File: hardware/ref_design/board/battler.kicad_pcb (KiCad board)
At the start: 2 copper layers, 71.4 x 127.7 mm, 173 parts, among them J1 TYPE-C-31-M-12, J2 53261-0271, J3 FH12-50S-0.5SH(55), J4 53261-0271, J5 SWD, J6 UART, J7 DEBUG PADS, Q1 2N7002, Q2 AO3401A, Q3 2N7002, Q4 2N7002, Q5 AO3400A, Q6 AO3400A, SW1 P1 UP, SW10 P2 DOWN, SW11 P2 LEFT, SW12 P2 RIGHT, SW13 P2 A, SW14 P2 B, SW15 P2 X, SW16 P2 Y, SW18 BOOTSEL, SW19 RESET, SW2 P1 DOWN, SW20 P1 SELECT, SW21 P1 START / PWR, SW22 P2 SELECT, SW23 P2 START, SW3 P1 LEFT, SW4 P1 RIGHT, SW5 P1 A, SW6 P1 B, SW7 P1 X, SW8 P1 Y, SW9 P2 UP, U1 SRV05-4, U2 TP4056-42-ESOP8, U3 ME6211C33M5G, U4 RP2354B, U6 MCP6002, U7 FM8002A, X1 12MHz

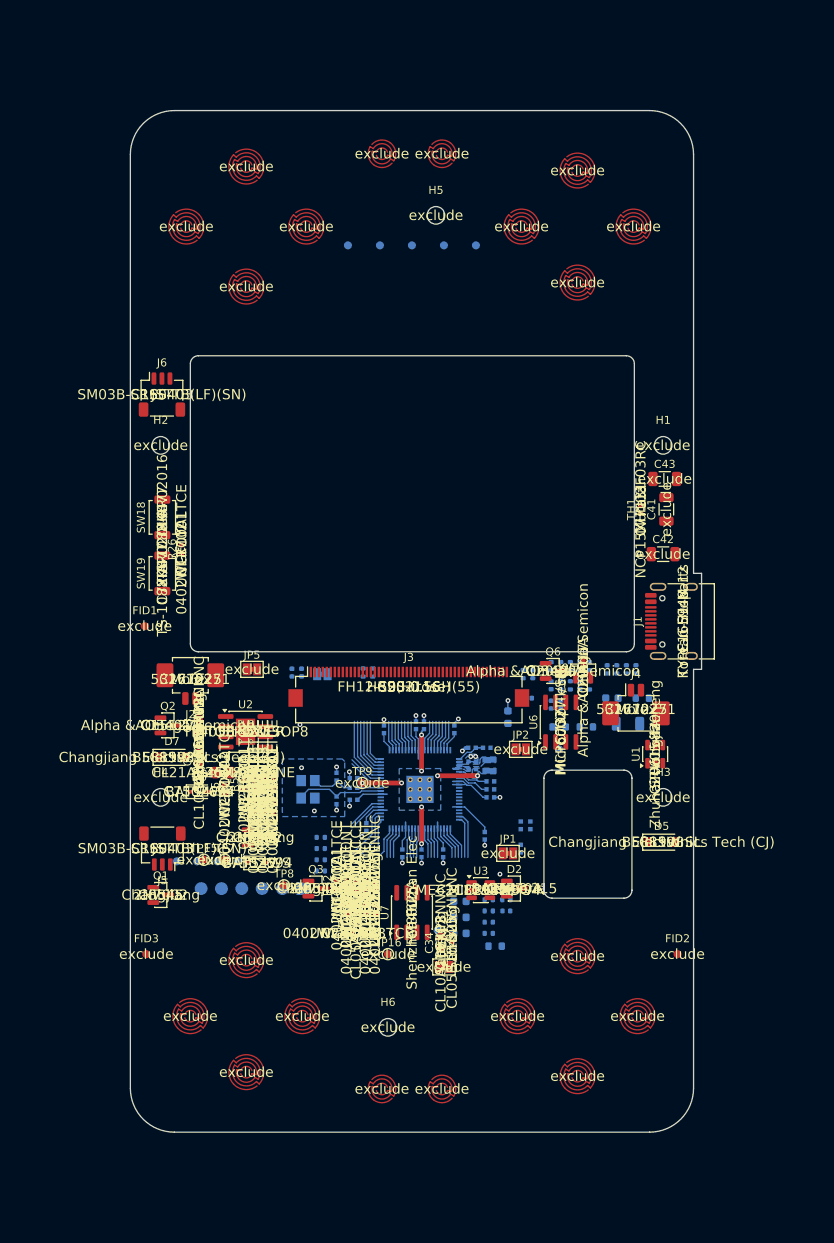
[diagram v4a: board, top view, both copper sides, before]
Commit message: WIP: row 19 layout, one-sided: no speaker, core in the left bezel (unrouted)
Since the one-sided-assembly ruling the work has been row 19, not row 18:
the speaker, J4 and the FM8002A circuit are out of design.py (GPIO8 and
GPIO11 unconnected), the cell sits in its hole, every SMT part is on the
front, and the RP2354B core moved from the back to the left bezel. Row 18
was ruled out on geometry first: with the core on the front it needs most of
one side bezel, and the speaker hole, J4 and three SOIC-8s had nowhere left.

Earlier row-19 placements (core in the right bezel) left 18-30 connections
open after Freerouting: J1's pads faced the cell hole with 1.3 mm to spare,
and seat 2's lines had to cross the whole board past the charger. This
commit has the core and the charger swapped, the hole's lead pocket cut to
1 mm and the original pin map; not routed yet.

Co-Authored-By: Claude Opus 5.5 <noreply@anthropic.com>
Claude-Session: https://claude.ai/code/session_01Y3mFMxLYqNeyyedvbYuRwX
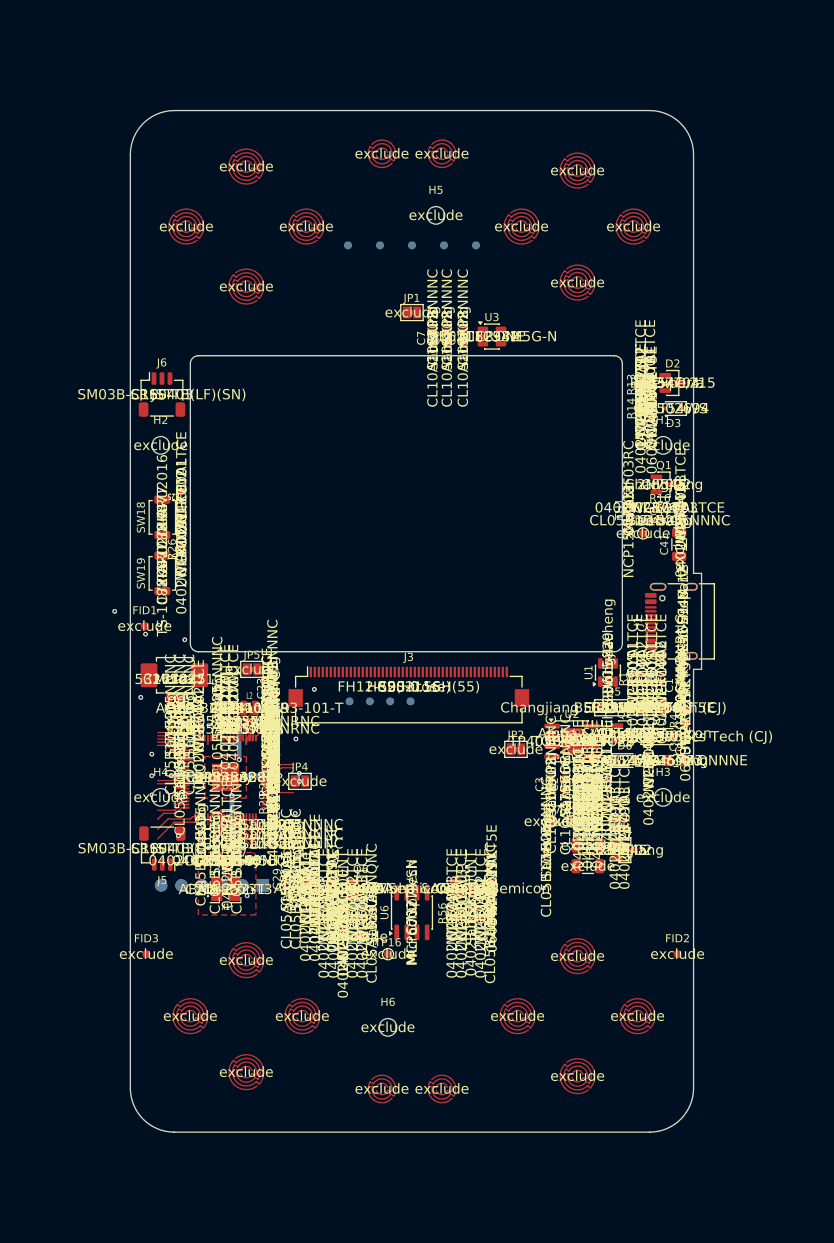
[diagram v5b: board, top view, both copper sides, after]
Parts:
- removed C34: 10u, Capacitor_SMD:C_0603_1608Metric
- removed C35: 100n, Capacitor_SMD:C_0402_1005Metric
- removed C37, C38: 4.7n, Capacitor_SMD:C_0402_1005Metric
- removed C39: 220n, Capacitor_SMD:C_0402_1005Metric
- removed C40: 1u, Capacitor_SMD:C_0402_1005Metric
- removed J4: 53261-0271, Connector_Molex:Molex_PicoBlade_53261-0271_1x02-1MP_P1.25mm_Horizontal
- removed JP3: Bridged, Jumper:SolderJumper-2_P1.3mm_Bridged_Pad1.0x1.5mm
- removed Q3: 2N7002, Package_TO_SOT_SMD:SOT-23
- removed R32, R33: 1k, Resistor_SMD:R_0402_1005Metric
- removed R34, R35: 20k, Resistor_SMD:R_0402_1005Metric
- removed R36, R37: 100k, Resistor_SMD:R_0402_1005Metric
- removed TP8: AMP_SHDN, TestPoint:TestPoint_Pad_D1.0mm
- removed U7: FM8002A, Package_SO:SOIC-8_3.9x4.9mm_P1.27mm
- C1, C10, C11, C12, C13, C14, C15, C16, C17, C18, C19, C20, C21, C22, C23, C24, C25, C26, C27, C28, C29, C30, C47, C48, C49, C5, C50, C51, C6, C7, C8, JP4, L2, R1, R13, R14, R15, R16, R17, R18, R19, R2, R20, R21, R22, R23, R25, R28, R29, R3, R38, R4, R41, R42, R47, R48, R49, R50, R51, R52, R53, R54, R55, R56, R57, R58, R59, R60, R61, TP10, TP6, U4, X1: moved to F.Cu
- TP9: moved to B.Cu
- moved Q1 81.2 mm to (131.5, 82.9)
- moved D3 77.1 mm to (132.7, 73.4), turned to 180 degrees
- moved C7 74.5 mm to (102.6, 64.6), turned to 90 degrees
- moved C6 72.4 mm to (104.4, 64.6), turned to 90 degrees
- moved C5 70.4 mm to (106.4, 64.6), turned to 90 degrees
- moved R38 69.8 mm to (130.0, 73.6), turned to 90 degrees
- moved U3 69.2 mm to (110.0, 64.4)
- moved JP1 68.7 mm to (100.0, 61.4)
- moved R13 67.1 mm to (128.6, 70.4), turned to 90 degrees
- moved R42 66.9 mm to (129.8, 70.4), turned to 90 degrees
- moved D2 66.2 mm to (132.6, 70.2)
- moved R14 65.6 mm to (128.6, 73.4), turned to 90 degrees
- moved D7 61.1 mm to (131.0, 114.4)
- moved R25 59.9 mm to (71.2, 84.4)
- moved R16 57.3 mm to (131.0, 85.8), turned to 0 degrees
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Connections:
- U4 pad 6: AUDIO_PWM -> unconnected-(U4-GPIO8-Pad6)
- U4 pad 9: AMP_EN -> unconnected-(U4-GPIO11-Pad9)
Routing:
- net +3V3: track 37.8 -> 16.3 mm, vias 0 -> 1
- net GND: track 12.9 -> 4.69 mm
- net /MCU/REV1: track 6.94 -> 1.31 mm
- net PWR_HOLD: track 5.81 -> 0.44 mm
- net RUN: track 8.71 -> 4.21 mm, vias 0 -> 1
- net P1_UP: track 8.09 -> 3.69 mm
- net P1_DOWN: track 7.46 -> 3.17 mm
- net P1_LEFT: track 6.84 -> 2.64 mm
- net P1_RIGHT: track 6.21 -> 2.11 mm
- net LCD_TE: track 5.59 -> 1.59 mm
- net CC1_SENSE: track 3.85 -> 0.00 mm
- net BL_PWM: track 3.85 -> 0.00 mm
- net P1_A: track 3.85 -> 0.00 mm
- net CC2_SENSE: track 3.85 -> 0.00 mm
- net VBAT_SENSE: track 3.85 -> 0.00 mm
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- added copper zone on F.Cu, net +1V1
- added copper zone on F.Cu, net +3V3
- added copper zone on F.Cu, net GND
- added copper zone on F.Cu, net VREG_LX
- removed copper zone on B.Cu, net +1V1
- removed copper zone on B.Cu, net +3V3
- removed copper zone on B.Cu, net GND
- removed copper zone on B.Cu, net VREG_LX
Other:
- outline, holes or cut-outs redrawn

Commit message: WIP: row 19 with shift registers and rows 1, 4, 16; 2 nets unrouted
The cell in a 54.0 x 37.0 mm hole, no speaker, every machine-placed part on
the top. New since the last WIP: each seat's D-pad and A/B/X/Y through a
74HC165 (SN74HC165PWR, chained, SR_PL/SR_CLK/SR_DATA on GPIO28-30, 10k
arrays); seat 2's Start powers on too (D8, R62, Q7, R63; P2_START on
GPIO34); Start/Select on 4 mm metal dome footprints; the BQ24073 power-path
charger in place of the TP4056 and its load sharing (pin reviews written);
the LDO beside the core; side screws at case (+-31.4, +-36); J1 at case
y -11. GPIO8 and GPIO11 (audio) unconnected.

Checks: check_netlist, check_pins and ERC pass (0). DRC: 0 errors, 8
cosmetic silkscreen warnings, 2 unconnected: QSPI_SS (U4 pin 75 to its
3.5 mm stub) and P1_SELECT (U4 pin 44 to SW20). check_fit: 17, all from
the case not knowing the moved screws, J1 and the dome vents yet.

Co-Authored-By: Claude Opus 5.5 <noreply@anthropic.com>
Claude-Session: https://claude.ai/code/session_01Y3mFMxLYqNeyyedvbYuRwX
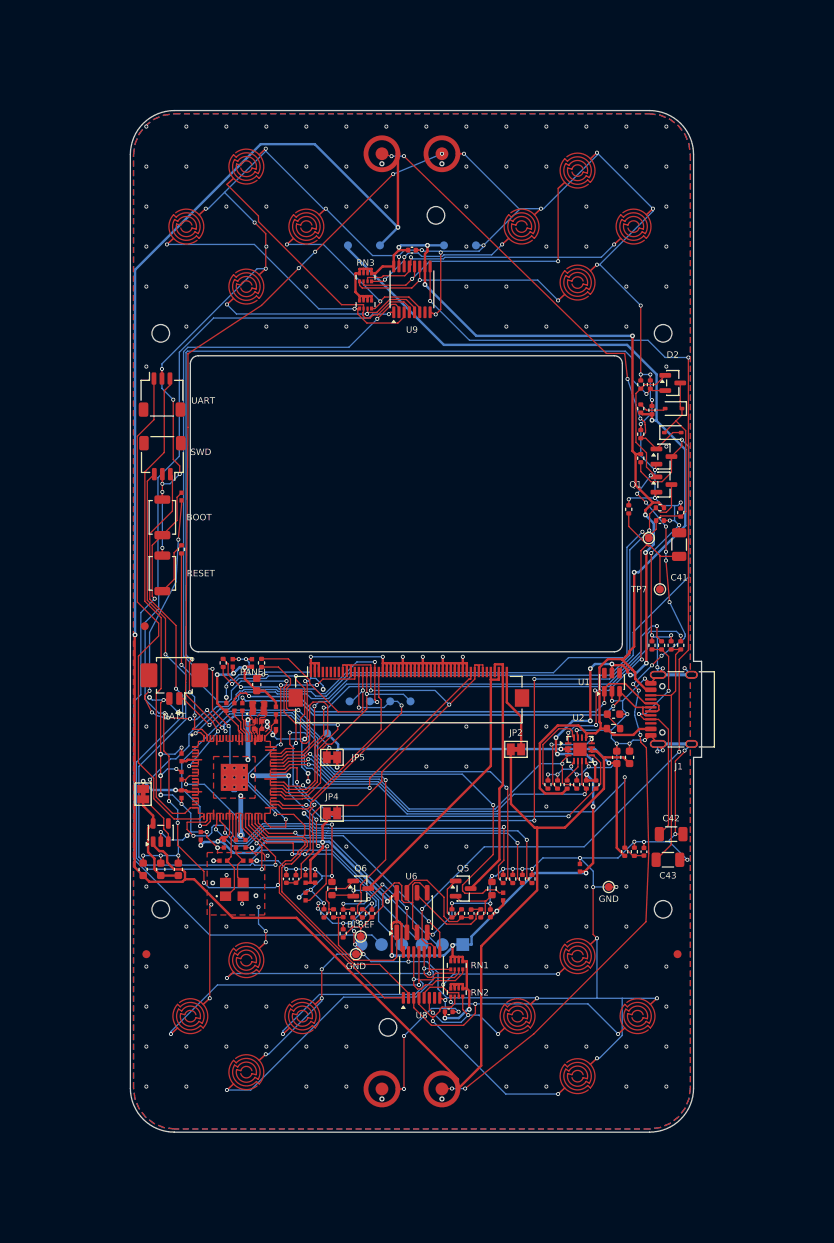
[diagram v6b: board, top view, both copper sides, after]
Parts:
- removed C9: 22u, Capacitor_SMD:C_0805_2012Metric
- removed D5, D7: B5819W, Diode_SMD:D_SOD-123
- removed D6: BAT54WS, Diode_SMD:D_SOD-323
- removed Q2: AO3401A, Package_TO_SOT_SMD:SOT-23
- removed Q4: 2N7002, Package_TO_SOT_SMD:SOT-23
- removed R39: 5.6k, Resistor_SMD:R_0402_1005Metric
- removed R40: 150k, Resistor_SMD:R_0402_1005Metric
- removed R47: 0.1, Resistor_SMD:R_1206_3216Metric
- removed R6: 10k, Resistor_SMD:R_0402_1005Metric
- added C52: 100n, Capacitor_SMD:C_0402_1005Metric, F.Cu at (104.6, 148.8)
- added C53: 100n, Capacitor_SMD:C_0402_1005Metric, F.Cu at (100.0, 53.6)
- added D8: BAT54WS, Diode_SMD:D_SOD-323, F.Cu at (132.6, 76.4)
- added Q7: 2N7002, Package_TO_SOT_SMD:SOT-23, F.Cu at (131.5, 79.4)
- added R62: 33k, Resistor_SMD:R_0402_1005Metric, F.Cu at (128.6, 76.6)
- added R63: 100k, Resistor_SMD:R_0402_1005Metric, F.Cu at (128.6, 79.6)
- added R64: 3.3k, Resistor_SMD:R_0402_1005Metric, F.Cu at (118.2, 120.4)
- added RN1: 10k, Resistor_SMD:R_Array_Convex_4x0402, F.Cu at (105.6, 143.0)
- added RN2: 10k, Resistor_SMD:R_Array_Convex_4x0402, F.Cu at (105.6, 146.4)
- added RN3: 10k, Resistor_SMD:R_Array_Convex_4x0402, F.Cu at (94.2, 57.0)
- added RN4: 10k, Resistor_SMD:R_Array_Convex_4x0402, F.Cu at (94.2, 60.4)
- added U8: SN74HC165PWR, Package_SO:TSSOP-16_4.4x5mm_P0.65mm, F.Cu at (101.2, 144.2)
- added U9: SN74HC165PWR, Package_SO:TSSOP-16_4.4x5mm_P0.65mm, F.Cu at (100.0, 58.5)
- C47: value 100n -> 1u
- R38: value 1k -> 10k; footprint Resistor_SMD:R_0603_1608Metric -> Resistor_SMD:R_0402_1005Metric
- SW20, SW21, SW22: footprint battler:DSL_button_3ring -> battler:Dome_4mm_Round
- SW23: value P2 START -> P2 START / PWR; footprint battler:DSL_button_3ring -> battler:Dome_4mm_Round
- TH1: value 10k B3380 -> 10k B3950
- TP7: value LS_GATE -> CHG_TEMP
- U2: value TP4056-42-ESOP8 -> BQ24073RGTR; footprint battler:SOIC-8-1EP_3.9x4.9mm_P1.27mm_EP2.41x3.3mm_ThermalVias_0.3mm -> Package_DFN_QFN:VQFN-16-1EP_3x3mm_P0.5mm_EP1.68x1.68mm
- moved C5 77.5 mm to (66.4, 131.0)
- moved C6 75.4 mm to (68.6, 131.0)
- moved U3 74.6 mm to (68.6, 126.4), turned to 90 degrees
- moved C7 73.6 mm to (70.8, 131.0)
- moved JP1 68.9 mm to (66.4, 121.6), turned to 90 degrees
- moved TP3 61.9 mm to (89.4, 114.0)
- moved J5 48.8 mm to (68.8, 79.6)
- moved C8 47.5 mm to (129.0, 128.8)
- moved R23 43.7 mm to (111.4, 134.4)
- moved TP7 32.0 mm to (131.0, 96.0)
- moved R50 27.2 mm to (113.8, 132.2)
- moved R51 27.2 mm to (115.0, 132.2)
- moved J7 26.1 mm to (100.0, 140.4)
- moved R48 24.7 mm to (111.4, 132.2)
- moved R49 24.7 mm to (112.6, 132.2)
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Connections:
- R43 pad 2: /USB_Charger/CHG_CE -> /USB_Charger/CHG_EN1
- R5 pad 1: /USB_Charger/CHG_PROG -> /USB_Charger/CHG_ISET
- R9 pad 1: CHG_DONE_N -> CHG_PG_N
- SW1 pad 1: P1_UP -> /Buttons/P1_UP
- SW10 pad 1: P2_DOWN -> /Buttons/P2_DOWN
- SW11 pad 1: P2_LEFT -> /Buttons/P2_LEFT
- SW12 pad 1: P2_RIGHT -> /Buttons/P2_RIGHT
- SW13 pad 1: P2_A -> /Buttons/P2_A
- SW14 pad 1: P2_B -> /Buttons/P2_B
- SW15 pad 1: P2_X -> /Buttons/P2_X
- SW16 pad 1: P2_Y -> /Buttons/P2_Y
- SW2 pad 1: P1_DOWN -> /Buttons/P1_DOWN
- SW23 pad 1: P2_START -> P2_START_RAW
- SW23 pad 2: GND -> VSYS
- SW3 pad 1: P1_LEFT -> /Buttons/P1_LEFT
- SW4 pad 1: P1_RIGHT -> /Buttons/P1_RIGHT
- SW5 pad 1: P1_A -> /Buttons/P1_A
- SW6 pad 1: P1_B -> /Buttons/P1_B
- SW7 pad 1: P1_X -> /Buttons/P1_X
- SW8 pad 1: P1_Y -> /Buttons/P1_Y
- SW9 pad 1: P2_UP -> /Buttons/P2_UP
- TP7 pad 1: /USB_Charger/LS_GATE -> /USB_Charger/CHG_TEMP
- U2 pad 2: /USB_Charger/CHG_PROG -> VBAT
- U2 pad 3: GND -> VBAT
- U2 pad 4: VBUS -> CHG_OFF
- U2 pad 5: VBAT -> GND
- U2 pad 6: CHG_DONE_N -> /USB_Charger/CHG_EN1
- U2 pad 7: CHG_STAT_N -> CHG_PG_N
- U2 pad 8: /USB_Charger/CHG_CE -> GND
- U2 pad 9: GND -> CHG_STAT_N
- U4 pad 1: P2_UP -> unconnected-(U4-GPIO4-Pad1)
- U4 pad 11: P2_A -> unconnected-(U4-GPIO12-Pad11)
- U4 pad 12: P2_B -> unconnected-(U4-GPIO13-Pad12)
- U4 pad 13: P2_X -> unconnected-(U4-GPIO14-Pad13)
- U4 pad 14: P2_Y -> unconnected-(U4-GPIO15-Pad14)
- U4 pad 17: CHG_STAT_N -> unconnected-(U4-GPIO17-Pad17)
- U4 pad 18: CHG_DONE_N -> unconnected-(U4-GPIO18-Pad18)
- U4 pad 19: CHG_OFF -> unconnected-(U4-GPIO19-Pad19)
- U4 pad 2: P2_DOWN -> unconnected-(U4-GPIO5-Pad2)
- U4 pad 3: P2_LEFT -> unconnected-(U4-GPIO6-Pad3)
- U4 pad 36: P1_UP -> SR_PL
- U4 pad 37: P1_DOWN -> SR_CLK
- U4 pad 38: P1_LEFT -> SR_DATA
- U4 pad 39: P1_RIGHT -> unconnected-(U4-GPIO31-Pad39)
- U4 pad 4: P2_RIGHT -> unconnected-(U4-GPIO7-Pad4)
- U4 pad 43: P1_Y -> P2_START
- U4 pad 52: P1_B -> CHG_STAT_N
- U4 pad 53: P1_X -> CHG_PG_N
- U4 pad 54: P1_A -> CHG_OFF
- U4 pad 8: P2_START -> unconnected-(U4-GPIO10-Pad8)
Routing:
- net GND: track 4.69 -> 716.9 mm, vias 22 -> 251
- net +3V3: track 16.3 -> 303.9 mm, vias 1 -> 31
- net VSYS: track 0.00 -> 259.2 mm, vias 0 -> 2
- net SR_PL: track 0.00 -> 148.0 mm, vias 0 -> 6
- net SR_CLK: track 0.00 -> 140.5 mm, vias 0 -> 4
- net /Buttons/SR_CHAIN: track 0.00 -> 135.9 mm, vias 0 -> 4
- net VBUS: track 0.00 -> 131.9 mm, vias 0 -> 2
- net /Power/PWR_EN: track 0.00 -> 119.7 mm, vias 0 -> 2
- net PWR_HOLD: track 0.44 -> 114.9 mm, vias 0 -> 4
- net PWR_BTN_RAW: track 0.00 -> 112.3 mm, vias 0 -> 14
- net P2_START: track 0.00 -> 106.2 mm, vias 0 -> 4
- net SWCLK: track 4.51 -> 106.5 mm, vias 0 -> 3
- net SWDIO: track 4.56 -> 105.3 mm, vias 0 -> 2
- net QSPI_SS: track 0.00 -> 100.2 mm, vias 0 -> 9
- net P2_SELECT: track 0.00 -> 96.0 mm, vias 0 -> 6
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- added copper zone on B.Cu, net GND
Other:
- outline, holes or cut-outs redrawn
- board text added: "+"
- board text added: "1V1"
- board text added: "2 LAYERS 1.6 MM ENIG"
- board text added: "3V3"
- board text added: "BATT"
- board text added: "BLREF"
- board text added: "BOOT"
- board text added: "CS"
- board text added: "DC"
- board text added: "GND"
- board text added: "MOSI"
- board text added: "PANEL"
- board text added: "RESET"
- board text added: "REV 1"
- board text added: "SCK"
- board text added: "SWD"
- board text added: "SWD PADS"
- board text added: "TWO-PLAYER HANDHELD REF-A"
- board text added: "UART"
- board text added: "VBAT"
- board text added: "VBUS"
- board text added: "VSYS"

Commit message: ref_design: the cell in the board (row 19), routed clean
The board with the cell in a 54.0 x 37.0 mm hole, no speaker, every
machine-placed part on the top, the D-pads and face buttons through two
74HC165s, rows 1, 4 and 16, side screws at case (+-31.4, +-36), J1 at case
y -11. route.py now gives each metal-dome contact a via in the gap between
its centre pad and ring (the centre pad's only way out), which closed
P1_SELECT; the seeded router's seed 6 then came out clean.

check_netlist, check_pins, ERC: pass. DRC: 0 errors, 0 unconnected (8
cosmetic silkscreen warnings). check_fit: 17, all from the case not knowing
the moved screws, J1 and the dome vents yet (case/CELLCUT_FOR_CASE.md).

Co-Authored-By: Claude Opus 5.5 <noreply@anthropic.com>
Claude-Session: https://claude.ai/code/session_01Y3mFMxLYqNeyyedvbYuRwX
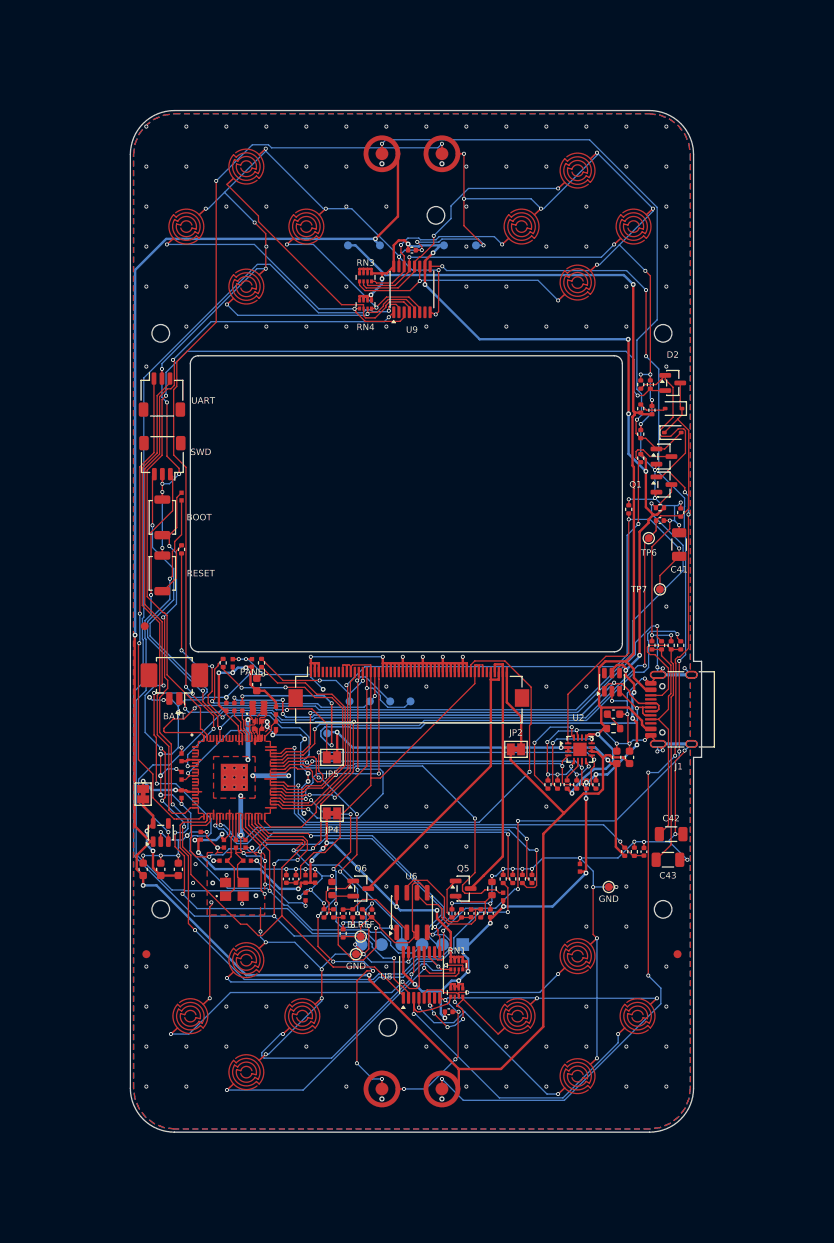
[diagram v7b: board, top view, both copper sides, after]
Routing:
- net P1_SELECT: track 0.00 -> 55.4 mm, vias 0 -> 8
- net LCD_RST: track 32.4 -> 59.5 mm
- net SR_CLK: track 140.5 -> 167.0 mm, vias 4 -> 5
- net P2_START_RAW: track 58.2 -> 76.5 mm, vias 4 -> 2
- net PWR_BTN_RAW: track 112.3 -> 130.2 mm, vias 14 -> 6
- net /MCU/REV1: track 71.6 -> 54.5 mm
- net P2_START: track 106.2 -> 89.8 mm, vias 4 -> 2
- net VSYS: track 259.2 -> 242.9 mm, vias 2 -> 4
- net P2_SELECT: track 96.0 -> 111.4 mm
- net /MCU/REV0: track 54.5 -> 67.8 mm
- net USB_DM: track 57.2 -> 68.7 mm, vias 2 -> 4
- net VBAT_SENSE: track 67.9 -> 57.2 mm
- net PWR_BTN_N: track 85.9 -> 96.3 mm
- net /USB_Charger/CC2: track 31.3 -> 41.0 mm
- net LCD_MOSI_MCU: track 44.0 -> 34.5 mm
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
